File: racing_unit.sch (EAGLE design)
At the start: 68 parts, among them IC1 78M05, IC2 ATMega328P-AU, IC3 78M05, IC4 78M05, IC5 78M05, IC6 LM1117-3.3, Q1 BDX54C, Q2 BDX54C, Q3 16MHz, Q4 BDX54C, Q5 BDX54C, Q6 BSS138, Q7 BSS138, X1 COIL1, X2 COIL2, X3 COIL3, X4 COIL4, X5 QS-SENSOR, X6 SUPPLY

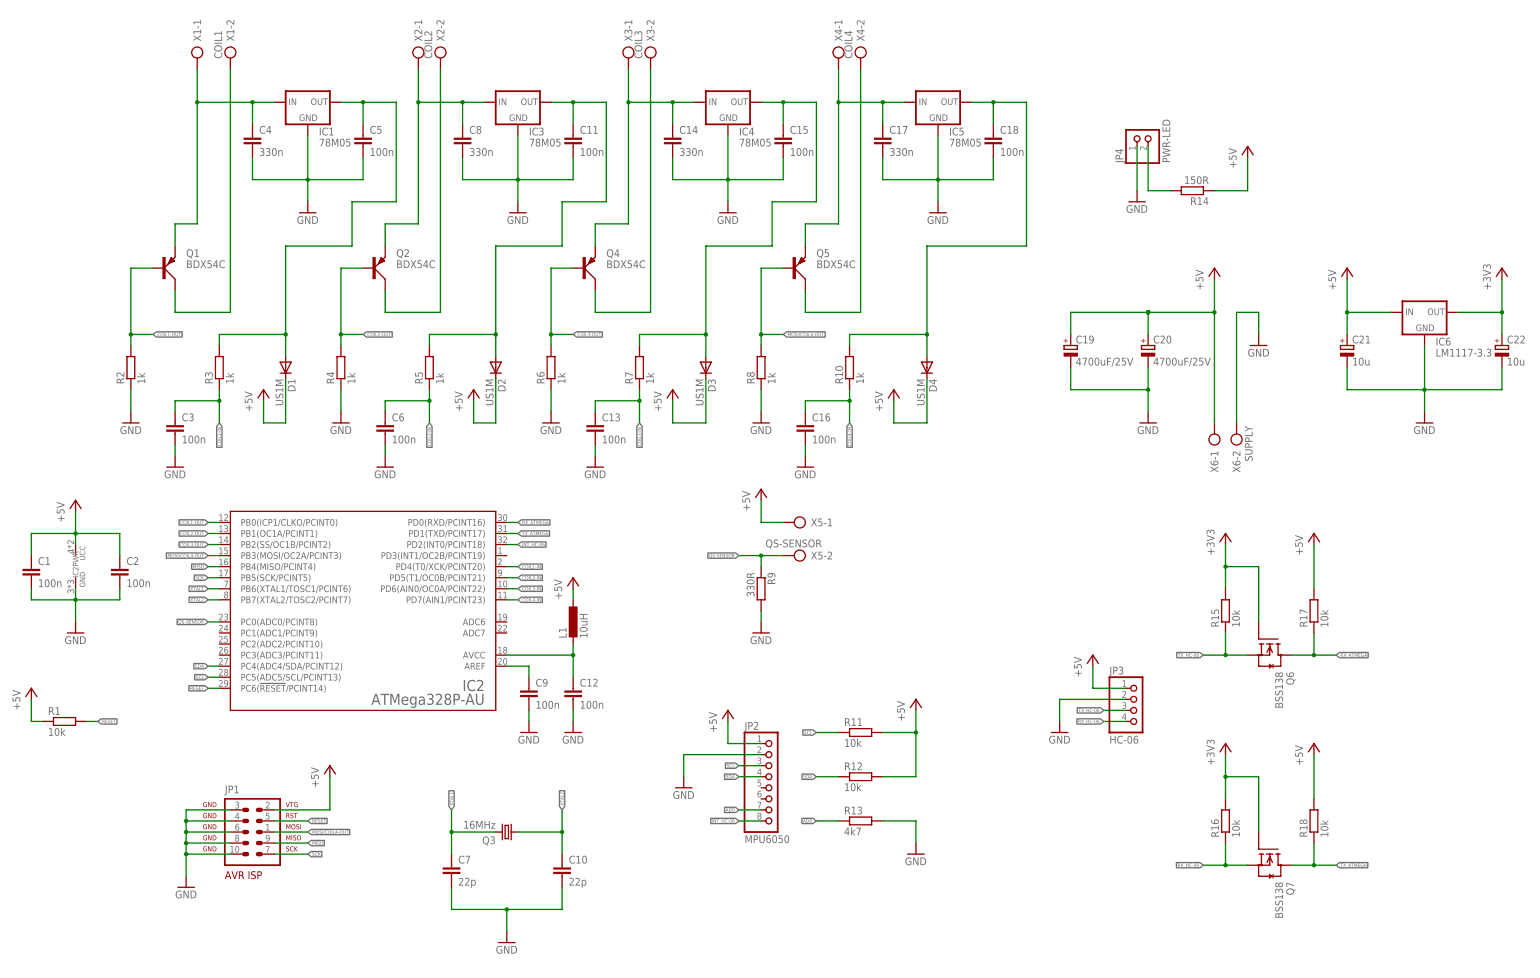
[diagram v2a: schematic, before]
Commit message: changed coil switches to mosfet's
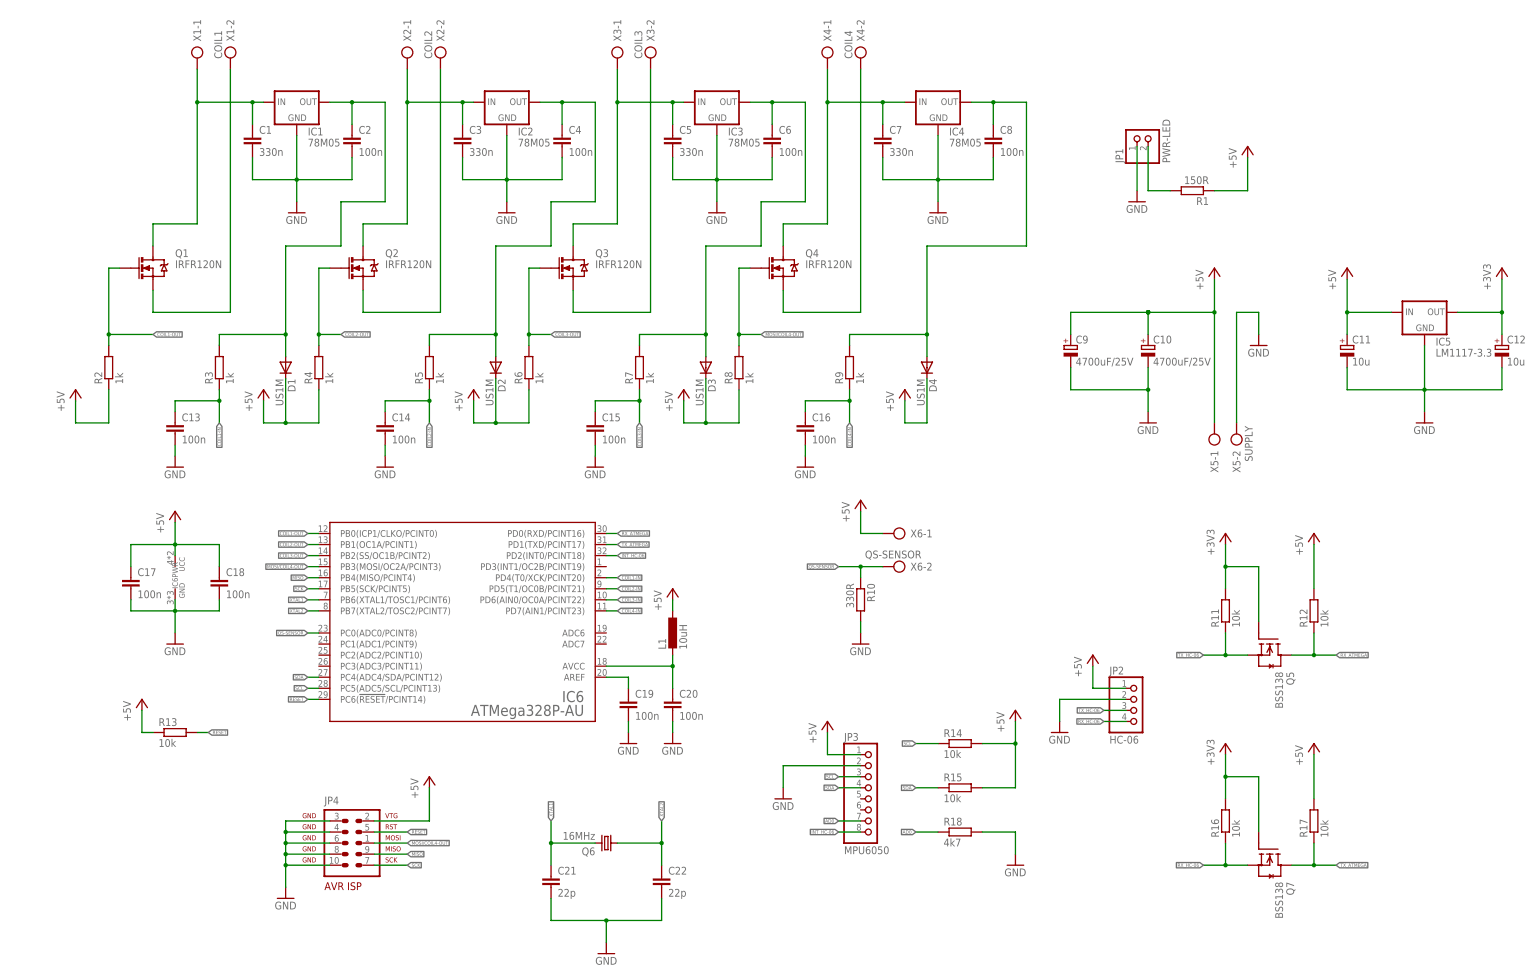
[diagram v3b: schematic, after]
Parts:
- C1, C3, C5: value 100n -> 330n
- C10: value 22p -> 4700uF/25V; device rcl:C-EUC0805 -> rcl:CPOL-EUE7.5-16
- C11, C12: value 100n -> 10u; device rcl:C-EUC0805 -> rcl:CPOL-EUA/3216-18R
- C14, C17, C4, C8: value 330n -> 100n
- C19, C20: value 4700uF/25V -> 100n; device rcl:CPOL-EUE7.5-16 -> rcl:C-EUC0805
- C21, C22: value 10u -> 22p; device rcl:CPOL-EUA/3216-18R -> rcl:C-EUC0805
- C7: value 22p -> 330n
- C9: value 100n -> 4700uF/25V; device rcl:C-EUC0805 -> rcl:CPOL-EUE7.5-16
- IC2: value ATMega328P-AU -> 78M05; device atmel_tiny24-44-84tiny48-88mega48-88-168-328:ATMEGA48/88/168/328-AU -> v-reg-2:LM1117TO252
- IC5: value 78M05 -> LM1117-3.3; device v-reg-2:LM1117TO252 -> v-reg-2:LM1117
- IC6: value LM1117-3.3 -> ATMega328P-AU; device v-reg-2:LM1117 -> atmel_tiny24-44-84tiny48-88mega48-88-168-328:ATMEGA48/88/168/328-AU
- JP1: value AVR-ISP-10ML -> PWR-LED; device atmel-1:AVR-ISP-10ML -> pinhead:PINHD-1X2
- JP2: value MPU6050 -> HC-06; device pinhead:PINHD-1X8 -> pinhead:PINHD-1X4
- JP3: value HC-06 -> MPU6050; device pinhead:PINHD-1X4 -> pinhead:PINHD-1X8
- JP4: value PWR-LED -> AVR-ISP-10ML; device pinhead:PINHD-1X2 -> atmel-1:AVR-ISP-10ML
- Q1, Q2, Q4: value BDX54C -> IRFR120N; device transistor-power:MJE2955 -> Simplex-DiscreteSemi:MOSFET-NCHANNEL_D-PAK
- Q3: value 16MHz -> IRFR120N; device crystal:CRYSTALHC49S -> Simplex-DiscreteSemi:MOSFET-NCHANNEL_D-PAK
- Q5: value BDX54C -> BSS138; device transistor-power:MJE2955 -> m-pad-2.1:BSS138
- Q6: value BSS138 -> 16MHz; device m-pad-2.1:BSS138 -> crystal:CRYSTALHC49S
- R1: value 10k -> 150R; device rcl:R-EU_M0805 -> resistor:R-EU_0204/5
- R10: value 1k -> 330R; device rcl:R-EU_M0805 -> resistor:R-EU_0204/5
- R13: value 4k7 -> 10k
- R14: value 150R -> 10k; device resistor:R-EU_0204/5 -> rcl:R-EU_M0805
- R18: value 10k -> 4k7
- R9: value 330R -> 1k; device resistor:R-EU_0204/5 -> rcl:R-EU_M0805
- X5: value QS-SENSOR -> SUPPLY
- X6: value SUPPLY -> QS-SENSOR
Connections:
- net +3V3: now also C12.+, IC5.OUT, Q5.G, R11.2; no longer C22.+, IC6.OUT, Q6.G, R15.2
- net +5V: now also C10.+, C11.+, C17.1, C18.1, C9.+, IC5.IN, IC6PWR.UCC, JP4.2, R13.1, R14.2, R15.2, R2.1, R4.1, R6.1, R8.1; no longer C1.1, C19.+, C2.1, C20.+, C21.+, IC2PWR.UCC, IC6.IN, JP1.2, R11.2, R14.1, R18.2
- net AD0: now also JP3.7, R18.1; no longer JP2.7, R13.1
- net COIL1-IN: now also C13.1, IC6IC.PD4(T0/XCK/PCINT20); no longer C3.1, IC2IC.PD4(T0/XCK/PCINT20)
- net COIL1-OUT: now also IC6IC.PB0(ICP1/CLKO/PCINT0), Q1.G; no longer IC2IC.PB0(ICP1/CLKO/PCINT0), Q1.B
- net COIL2-IN: now also C14.1, IC6IC.PD5(T1/OC0B/PCINT21); no longer C6.1, IC2IC.PD5(T1/OC0B/PCINT21)
- net COIL2-OUT: now also IC6IC.PB1(OC1A/PCINT1), Q2.G; no longer IC2IC.PB1(OC1A/PCINT1), Q2.B
- net COIL3-IN: now also C15.1, IC6IC.PD6(AIN0/OC0A/PCINT22); no longer C13.1, IC2IC.PD6(AIN0/OC0A/PCINT22)
- net COIL3-OUT: now also IC6IC.PB2(SS/OC1B/PCINT2), Q3.G; no longer IC2IC.PB2(SS/OC1B/PCINT2), Q4.B
- net COIL4-IN: now also IC6IC.PD7(AIN1/PCINT23), R9.1; no longer IC2IC.PD7(AIN1/PCINT23), R10.1
- net GND: now also C10.-, C11.-, C12.-, C19.2, C20.2, C21.2, C22.2, C9.-, IC2.GND, IC6PWR.GND, JP1.1, JP4.10, JP4.3, JP4.4, JP4.6, JP4.8, R10.2, R18.2, X5-2.KL; no longer C10.2, C11.2, C12.2, C19.-, C20.-, C21.-, C22.-, C9.2, IC2PWR.GND, IC6.GND, JP1.10, JP1.3, JP1.4, JP1.6, JP1.8, JP4.1, R13.2, R2.1, R4.1, R6.1, R8.1, R9.2, X6-2.KL
- net INT_HC-06: now also IC6IC.PD2(INT0/PCINT18), JP3.8; no longer IC2IC.PD2(INT0/PCINT18), JP2.8
- net MISO: now also IC6IC.PB4(MISO/PCINT4), JP4.9; no longer IC2IC.PB4(MISO/PCINT4), JP1.9
- net MOSI/COIL4-OUT: now also IC6IC.PB3(MOSI/OC2A/PCINT3), JP4.1, Q4.G; no longer IC2IC.PB3(MOSI/OC2A/PCINT3), JP1.1, Q5.B
- net N$1: now also C1.1, Q1.D; no longer C4.1, Q1.E
- net N$10: now also Q3.S; no longer Q4.C
- net N$11: now also Q2.S; no longer Q2.C
- net N$12: now also Q1.S; no longer Q1.C
- net N$13: now also JP1.2, R1.2; no longer JP4.2, R14.2
- net N$14: now also C2.1; no longer C5.1
- net N$15: now also C4.1, IC2.OUT; no longer C11.1, IC3.OUT
- net N$17: now also C8.1, IC4.OUT, R9.2; no longer C18.1, IC5.OUT, R10.2
- net N$2: now also C3.1, IC2.IN, Q2.D; no longer C8.1, IC3.IN, Q2.E
- net N$21: now also C6.1, IC3.OUT; no longer C15.1, IC4.OUT
- net N$3: now also C5.1, IC3.IN, Q3.D; no longer C14.1, IC4.IN, Q4.E
- net N$4: now also C7.1, IC4.IN, Q4.D; no longer C17.1, IC5.IN, Q5.E
- net N$5: now also C19.1, IC6IC.AREF; no longer C9.1, IC2IC.AREF
- net N$6: now also C20.1, IC6IC.AVCC; no longer C12.1, IC2IC.AVCC
- net N$9: now also Q4.S; no longer Q5.C
- net QS-SENSOR: now also IC6IC.PC0(ADC0/PCINT8), R10.1, X6-2.KL; no longer IC2IC.PC0(ADC0/PCINT8), R9.1, X5-2.KL
- net RESET: now also IC6IC.PC6(!RESET!/PCINT14), JP4.5, R13.2; no longer IC2IC.PC6(!RESET!/PCINT14), JP1.5, R1.2
- net RX_ATMEGA: now also IC6IC.PD0(RXD/PCINT16), Q5.D, R12.1; no longer IC2IC.PD0(RXD/PCINT16), Q6.D, R17.1
- net RX_HC-06: now also JP2.4; no longer JP3.4
- net SCK: now also IC6IC.PB5(SCK/PCINT5), JP4.7; no longer IC2IC.PB5(SCK/PCINT5), JP1.7
- net SCL: now also IC6IC.PC5(ADC5/SCL/PCINT13), JP3.3, R14.1; no longer IC2IC.PC5(ADC5/SCL/PCINT13), JP2.3, R11.1
- net SDA: now also IC6IC.PC4(ADC4/SDA/PCINT12), JP3.4, R15.1; no longer IC2IC.PC4(ADC4/SDA/PCINT12), JP2.4, R12.1
- net TX_ATMEGA: now also IC6IC.PD1(TXD/PCINT17), R17.1; no longer IC2IC.PD1(TXD/PCINT17), R18.1
- net TX_HC-06: now also JP2.3, Q5.S, R11.1; no longer JP3.3, Q6.S, R15.1
- net XTAL1: now also C21.1, IC6IC.PB6(XTAL1/TOSC1/PCINT6), Q6.2; no longer C7.1, IC2IC.PB6(XTAL1/TOSC1/PCINT6), Q3.2
- net XTAL2: now also C22.1, IC6IC.PB7(XTAL2/TOSC2/PCINT7), Q6.1; no longer C10.1, IC2IC.PB7(XTAL2/TOSC2/PCINT7), Q3.1
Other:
- moved on the sheet: C1, C13, C14, C15, C17, C18, C2, C3, C4, C5, C6, C7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

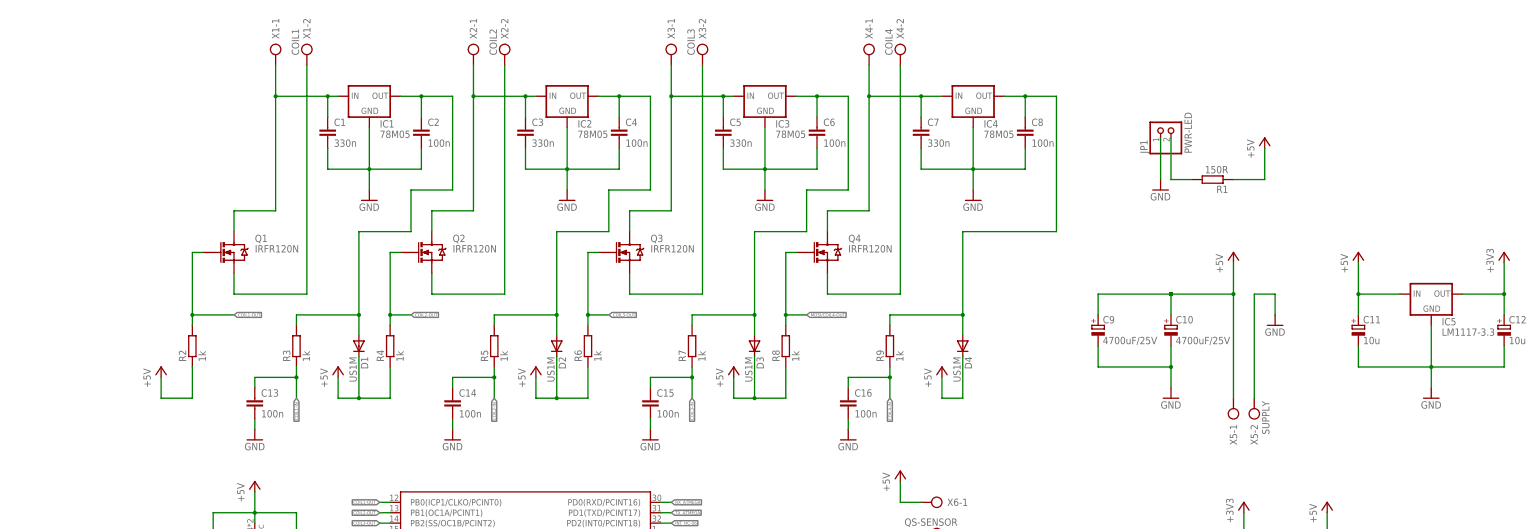
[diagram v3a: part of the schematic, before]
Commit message: added mosfet drivers and refactored launch control to be started by first spark kill
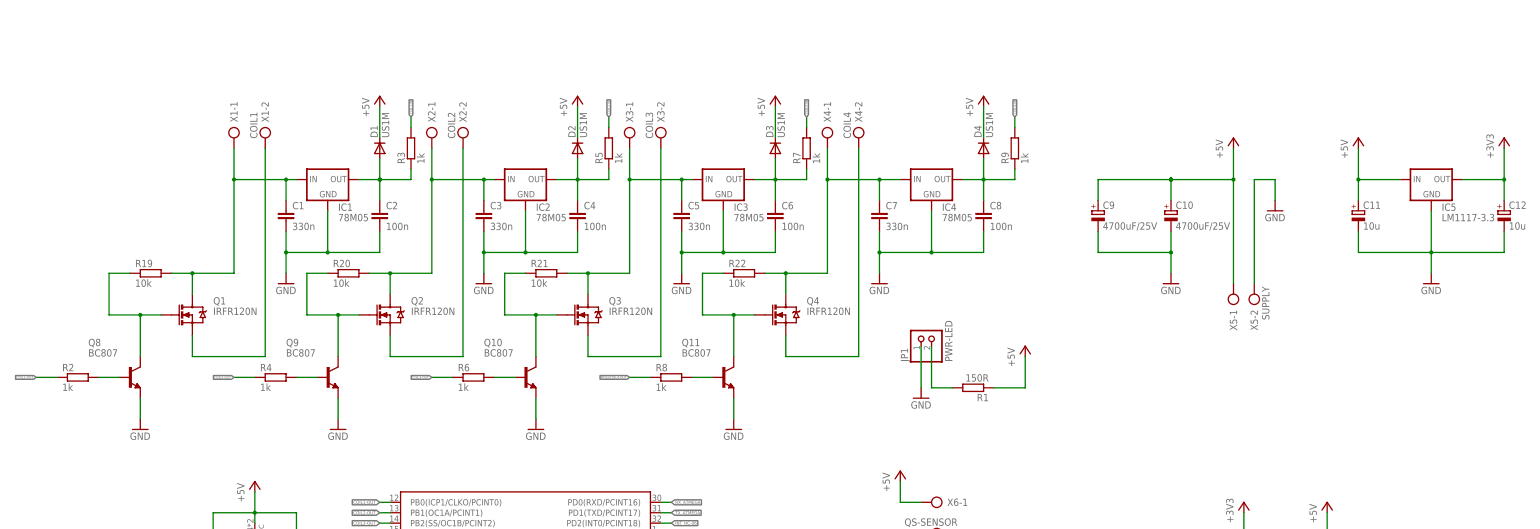
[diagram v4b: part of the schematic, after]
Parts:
- removed C13, C14, C15, C16: 100n, rcl:C-EUC0805
- added Q10, Q11, Q8, Q9: BC807, transistor-npn:BC817-16LT1SMD
- added R19, R20, R21, R22: 10k, rcl:R-EU_M0805
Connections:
- removed net N$21: C6.1, D3.A, IC3.OUT, R7.2
- new net N$123: Q1.G, Q8.C, R19.1
- new net N$124: Q2.G, Q9.C, R20.1
- new net N$125: Q10.C, Q3.G, R21.1
- new net N$126: Q11.C, Q4.G, R22.1
- new net N$16: Q10.B, R6.2
- new net N$18: C6.1, D3.A, IC3.OUT, R7.1
- new net N$19: Q11.B, R8.2
- new net N$7: Q8.B, R2.2
- new net N$8: Q9.B, R4.2
- net +5V: no longer R2.1, R4.1, R6.1, R8.1
- net COIL1-IN: now also R3.2; no longer C13.1, R3.1
- net COIL1-OUT: now also R2.1; no longer Q1.G, R2.2
- net COIL2-IN: now also R5.2; no longer C14.1, R5.1
- net COIL2-OUT: now also R4.1; no longer Q2.G, R4.2
- net COIL3-IN: now also R7.2; no longer C15.1, R7.1
- net COIL3-OUT: now also R6.1; no longer Q3.G, R6.2
- net COIL4-IN: now also R9.2; no longer C16.1, R9.1
- net GND: now also Q10.E, Q11.E, Q8.E, Q9.E; no longer C13.2, C14.2, C15.2, C16.2
- net MOSI/COIL4-OUT: now also R8.1; no longer Q4.G, R8.2
- net N$1: now also R19.2
- net N$14: now also R3.1; no longer R3.2
- net N$15: now also R5.1; no longer R5.2
- net N$17: now also R9.1; no longer R9.2
- net N$2: now also R20.2
- net N$3: now also R21.2
- net N$4: now also R22.2
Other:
- moved on the sheet: C1, C10, C11, C12, C2, C3, C4, C5, C6, C7, C8, C9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

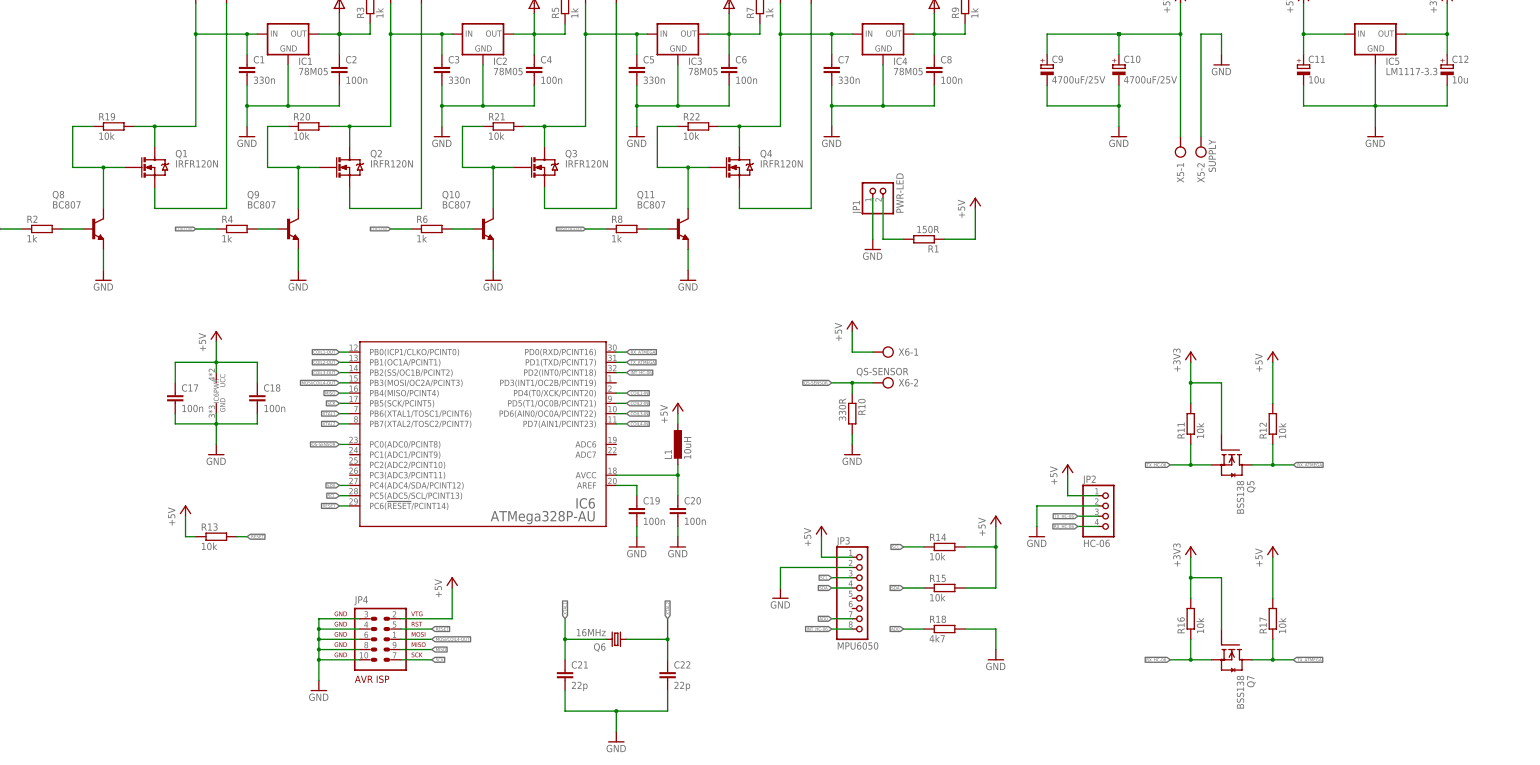
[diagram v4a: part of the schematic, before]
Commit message: improved rpm measurement
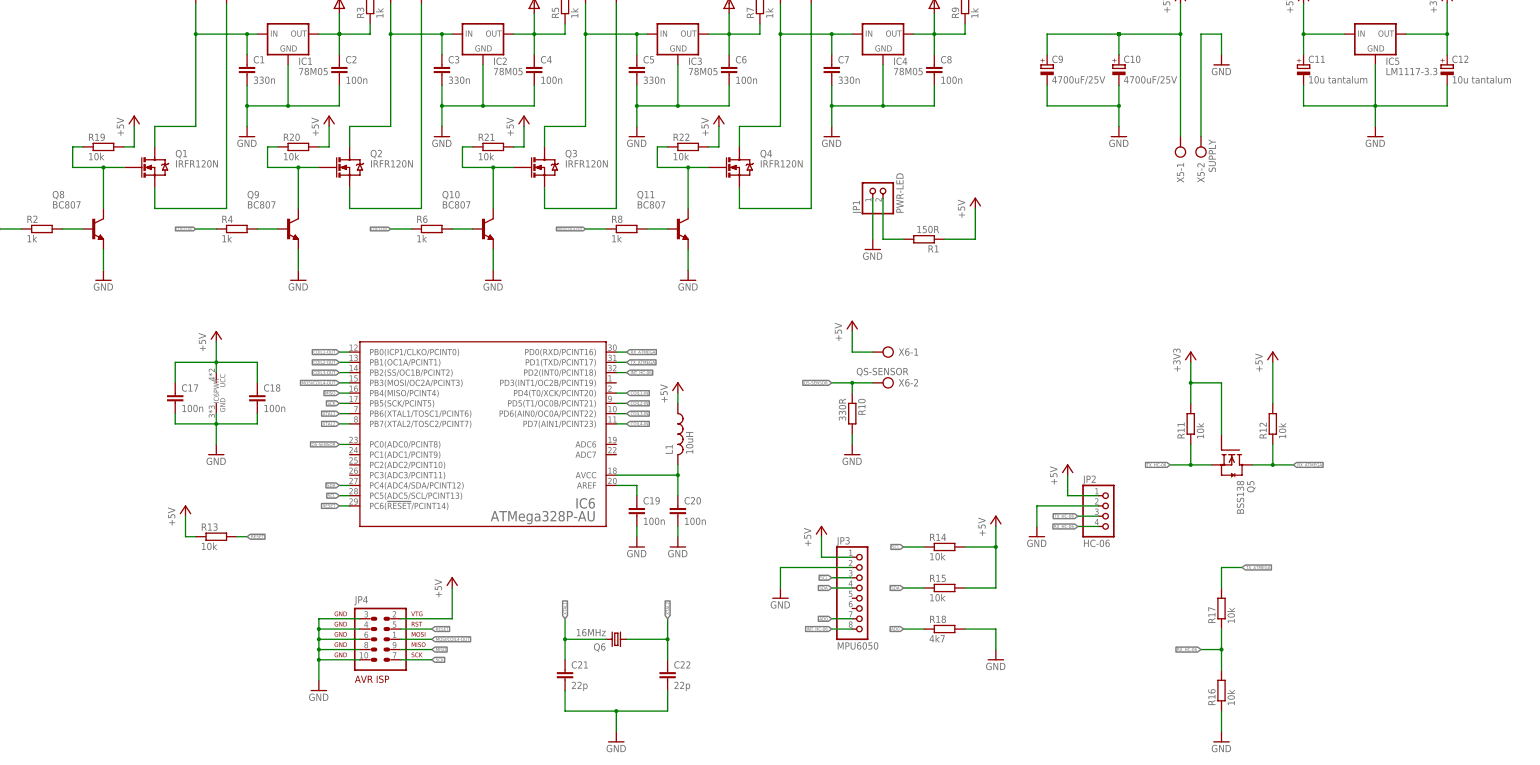
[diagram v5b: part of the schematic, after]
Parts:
- removed Q7: BSS138, m-pad-2.1:BSS138
- C11, C12: value 10u -> 10u tantalum
- L1: device rcl:L-EU0207/10 -> rcl:L-US0207/10
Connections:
- net +3V3: no longer Q7.G, R16.2
- net +5V: now also R19.2, R20.2, R21.2, R22.2; no longer R17.2
- net GND: now also R16.1
- net N$1: no longer R19.2
- net N$2: no longer R20.2
- net N$3: no longer R21.2
- net N$4: no longer R22.2
- net RX_HC-06: now also R16.2, R17.1; no longer Q7.S, R16.1
- net TX_ATMEGA: now also R17.2; no longer Q7.D, R17.1
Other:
- moved on the sheet: R16, R17, R19, R20, R21, R22
